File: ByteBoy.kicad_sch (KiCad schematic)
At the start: 10 parts, among them J1 1040310811 (SD Connector), J2 10118194-0001LF (USB-C Connec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, U1 ESP32-WROVER-E

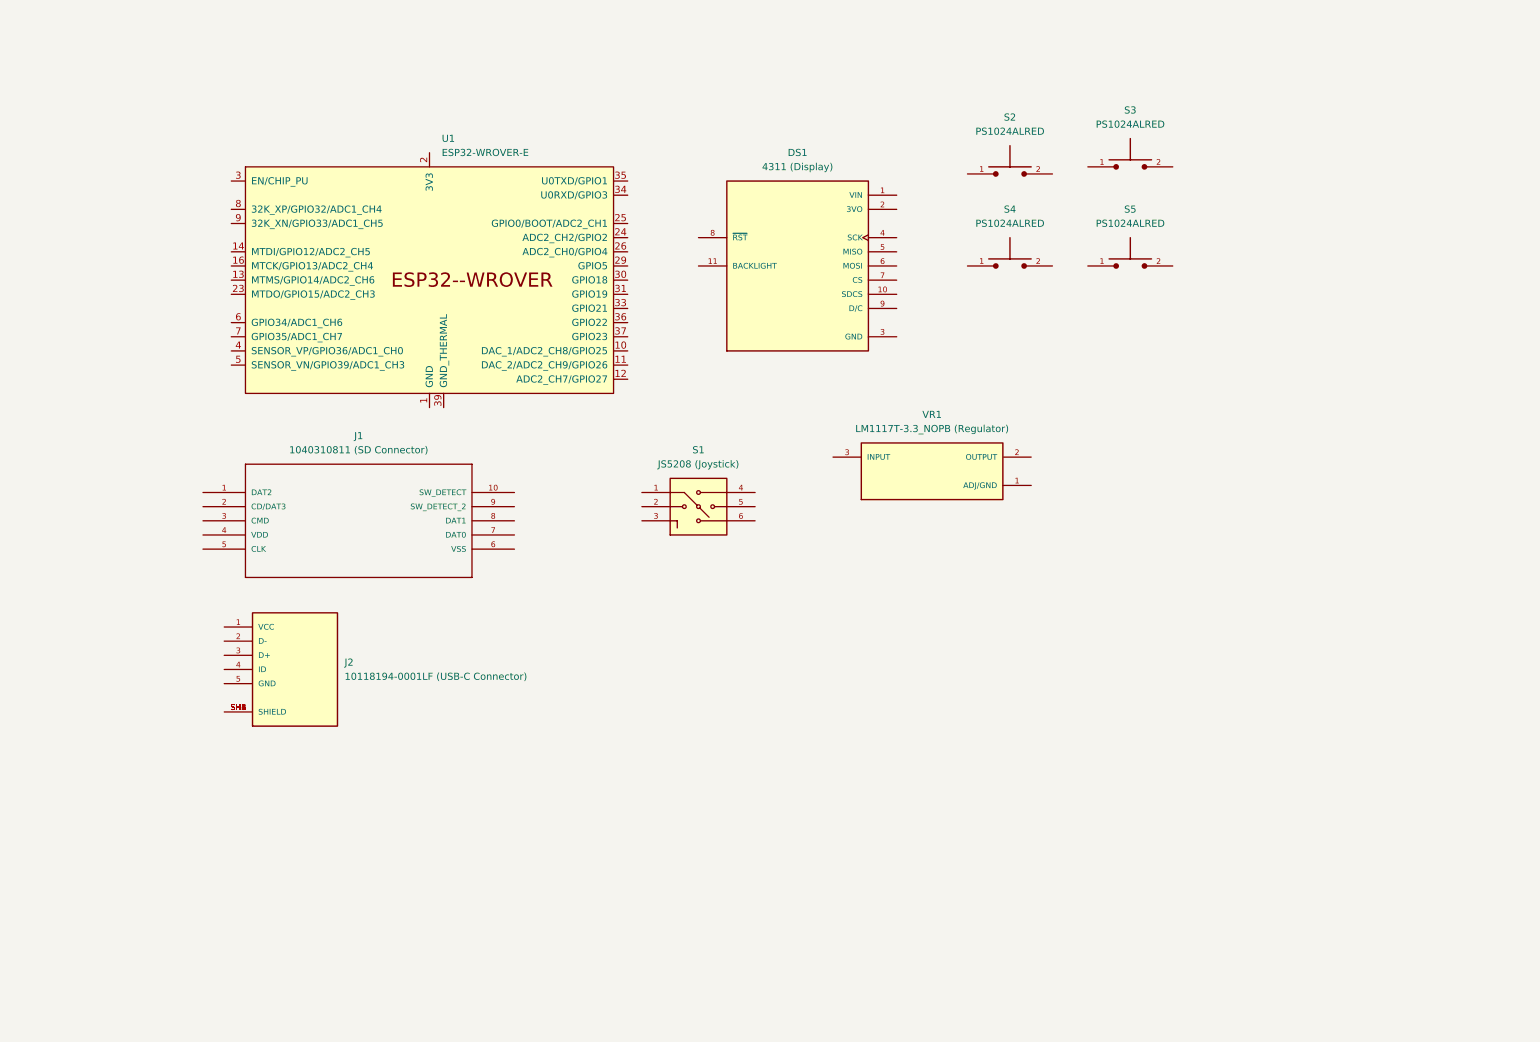
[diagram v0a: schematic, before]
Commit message: added usb to uart
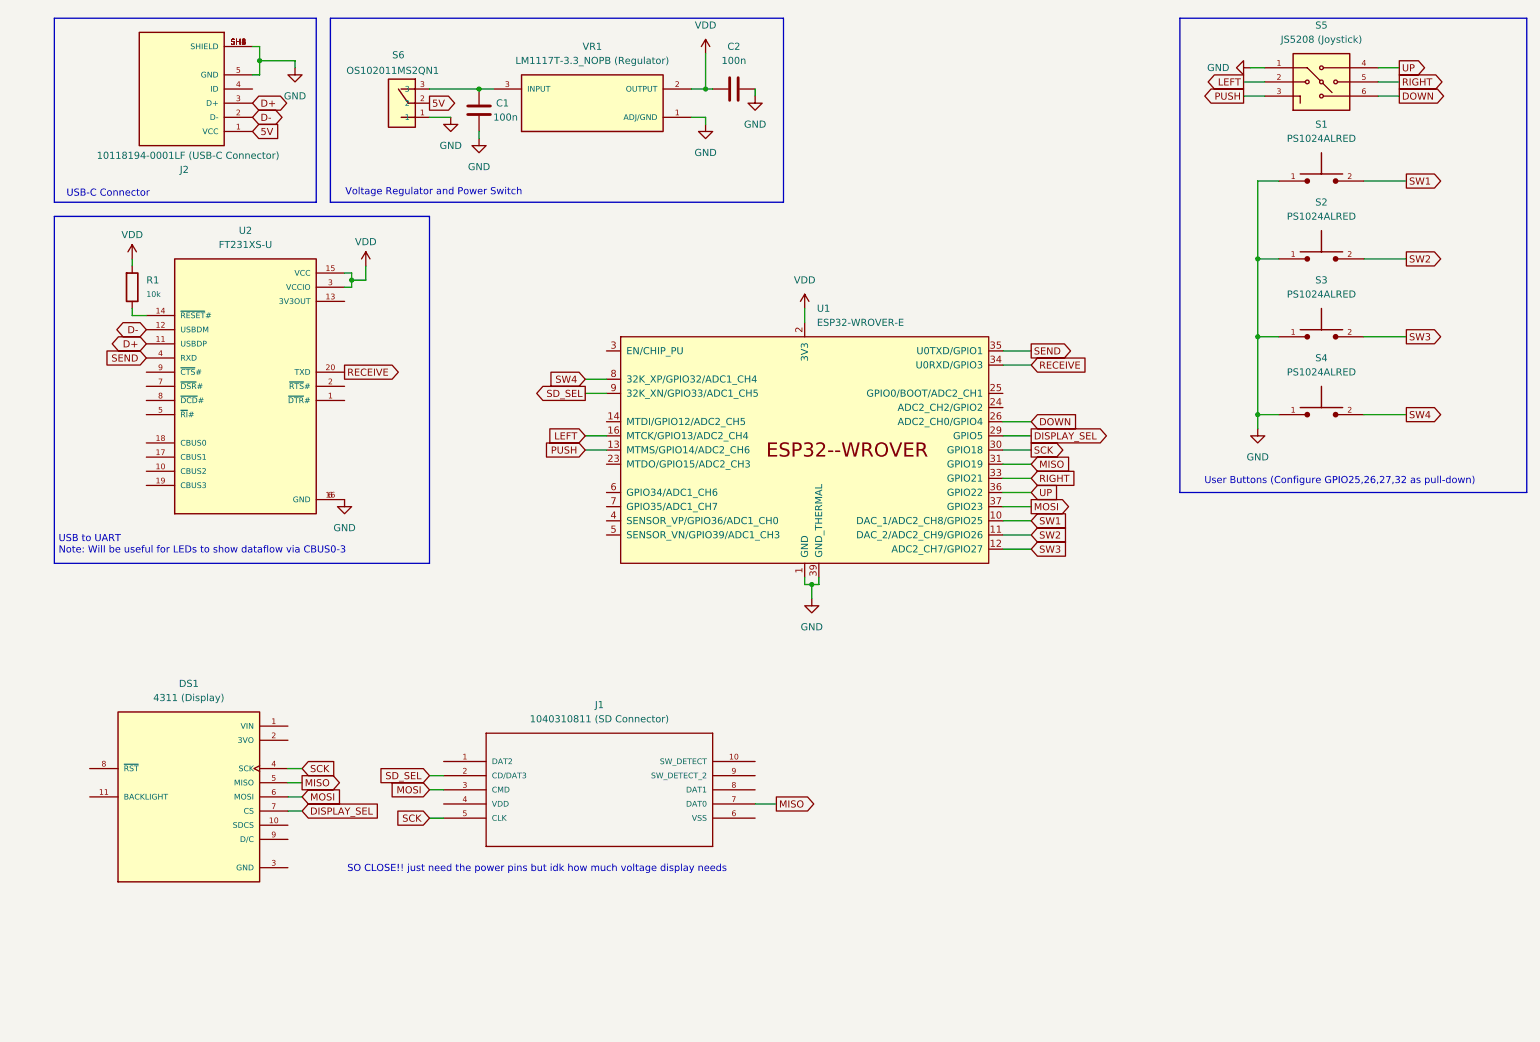
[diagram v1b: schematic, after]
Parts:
- added C1, C2: 100n, Capacitor_THT:C_Rect_L7.0mm_W2.5mm_P5.00mm, symbol enel200_uc_kicad7 (1):UC_C
- added R1: 10k, Resistor_THT:R_Axial_DIN0207_L6.3mm_D2.5mm_P7.62mm_Horizontal, symbol enel200_uc_kicad7 (1):UC_R
- added S6: OS102011MS2QN1, OS102011MS2QN1:SW_OS102011MS2QN1, symbol OS102011MS2QN1:OS102011MS2QN1
- added U2: FT231XS-U, FT231XS-U:SOP63P600X175-20N, symbol FT231XS-U:FT231XS-U
- renumbered S2 to S1, S3 to S2, S5 to S3, S1 to S5
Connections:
- net 5V: now reaches J2.1 (VCC)
- net 5V: now also S6.2
- net D-: now reaches J2.2 (D-)
- net D-: now also U2.12 (USBDM)
- net D+: now reaches J2.3 (D+)
- net D+: now also U2.11 (USBDP)
- net GND: now reaches J2.5 (GND)
- net GND: now also J2.SH1 (SHIELD), J2.SH2 (SHIELD), J2.SH3 (SHIELD), J2.SH4 (SHIELD), J2.SH5 (SHIELD), J2.SH6 (SHIELD), S1.1, S2.1, S3.1, S4.1, S5.1, U1.1 (GND), U1.15 (GND), U1.38 (GND), U1.39 (GND_THERMAL), VR1.1 (ADJ/GND), C1.1, C2.2, S6.1, U2.16 (GND), U2.6 (GND)
- net VDD: now reaches VR1.2 (OUTPUT)
- net VDD: now also U1.2 (3V3), C2.1, R1.1, U2.15 (VCC), U2.3 (VCCIO)
- net at VR1.3 (INPUT): now also C1.2, S6.3
- net SW1: now reaches U1.10 (DAC_1/ADC2_CH8/GPIO25)
- net SW1: now also S1.2
- net SW2: now reaches U1.11 (DAC_2/ADC2_CH9/GPIO26)
- net SW2: now also S2.2
- net SW3: now reaches U1.12 (ADC2_CH7/GPIO27)
- net SW3: now also S3.2
- net PUSH: now reaches U1.13 (MTMS/GPIO14/ADC2_CH6)
- net PUSH: now also S5.3
- net LEFT: now reaches U1.16 (MTCK/GPIO13/ADC2_CH4)
- net LEFT: now also S5.2
- net DOWN: now reaches U1.26 (ADC2_CH0/GPIO4)
- net DOWN: now also S5.6
- net DISPLAY_SEL: now reaches U1.29 (GPIO5)
- net DISPLAY_SEL: now also DS1.7 (CS)
- net SCK: now reaches U1.30 (GPIO18)
- net SCK: now also DS1.4 (SCK), J1.5 (CLK)
- net MISO: now reaches U1.31 (GPIO19)
- net MISO: now also DS1.5 (MISO), J1.7 (DAT0)
- net RIGHT: now reaches U1.33 (GPIO21)
- net RIGHT: now also S5.5
- net RECEIVE: now reaches U1.34 (U0RXD/GPIO3)
- net RECEIVE: now also U2.20 (TXD)
- net SEND: now reaches U1.35 (U0TXD/GPIO1)
- net SEND: now also U2.4 (RXD)
- net UP: now reaches U1.36 (GPIO22)
- net UP: now also S5.4
- net MOSI: now reaches U1.37 (GPIO23)
- net MOSI: now also DS1.6 (MOSI), J1.3 (CMD)
- net SW4: now reaches U1.8 (32K_XP/GPIO32/ADC1_CH4)
- net SW4: now also S4.2
- net SD_SEL: now reaches U1.9 (32K_XN/GPIO33/ADC1_CH5)
- net SD_SEL: now also J1.2 (CD/DAT3)
- new net: R1.2, U2.14 (~{RESET}#)
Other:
- note added: "SO CLOSE!! just need the power pins but idk how much voltage display needs"
- note added: "USB to UART Note: Will be useful for LEDs to show dataflow via CBUS0-3"
- note added: "USB-C Connector"
- note added: "User Buttons (Configure GPIO25,26,27,32 as pull-down)"
- note added: "Voltage Regulator and Power Switch"
- moved on the sheet: DS1, J1, J2, S1, S2, S3, S4, S5, U1, VR1

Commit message: adding decoupling
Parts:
- added C10: 1u, Capacitor_THT:C_Rect_L7.0mm_W2.5mm_P5.00mm, symbol enel200_uc_kicad7 (1):UC_C
- added C3, C5, C7, C9: 0.1u, Capacitor_THT:C_Rect_L7.0mm_W2.5mm_P5.00mm, symbol enel200_uc_kicad7 (1):UC_C
- added C4: 22u, Capacitor_THT:C_Rect_L7.0mm_W2.5mm_P5.00mm, symbol enel200_uc_kicad7 (1):UC_C
- added C6: 10u, Capacitor_THT:C_Rect_L7.0mm_W2.5mm_P5.00mm, symbol enel200_uc_kicad7 (1):UC_C
- added C8: 10uF, Capacitor_THT:C_Rect_L7.0mm_W2.5mm_P5.00mm, symbol enel200_uc_kicad7 (1):UC_C
- added D1, D2: UC_D, Diodes_THT:D_DO-35_SOD27_P2.54mm_Vertical_AnodeUp, symbol enel200_uc_kicad7 (1):UC_D
- added R2, R3: 5.1k, Resistor_THT:R_Axial_DIN0207_L6.3mm_D2.5mm_P7.62mm_Horizontal, symbol enel200_uc_kicad7 (1):UC_R
- added R4: 10k, Resistor_THT:R_Axial_DIN0207_L6.3mm_D2.5mm_P7.62mm_Horizontal, symbol enel200_uc_kicad7 (1):UC_R
- C1, C2: value 100n -> 10u
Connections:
- net 5V is gone; now on net +5V: J2.1 (VCC), S6.2
- net GND: now also C2.1, DS1.3 (GND), J1.6 (VSS), C10.2, C3.1, C5.2, C6.1, C7.2, C8.2, D1.1 (K), D2.1 (K); no longer C2.2
- net at U1.3 (EN/CHIP_PU): now also C10.1, R4.2
- net SD_DETECT: now reaches U1.4 (SENSOR_VP/GPIO36/ADC1_CH0)
- net SD_DETECT: now also J1.10 (SW_DETECT)
- net +3.3V: now reaches J1.4 (VDD)
- net +3.3V: now also C2.2, R1.1, U2.15 (VCC), U2.3 (VCCIO), VR1.2 (OUTPUT), C3.2, C4.1, C5.1, C9.1, R2.1, R4.1
- net +5V: now reaches DS1.1 (VIN)
- net +5V: now also C6.2, C7.1, C8.1, R3.1
- net DISPLAY_SEL renamed DISPLAY_SELECT
- net SD_SEL renamed SD_SELECT
- removed net VDD: C2.1, R1.1, U1.2 (3V3), U2.15 (VCC), U2.3 (VCCIO), VR1.2 (OUTPUT)
- new net: C4.2, C9.2, U1.2 (3V3)
- new net: D2.2 (A), R3.2
- new net: D1.2 (A), R2.2
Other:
- note added: "Display"
- note added: "User Buttons (Configure GPIO inputs as pull-down)"
- note added: "microSD card connector"
- note removed: "SO CLOSE!! just need the power pins but idk how much voltage display needs"
- note removed: "User Buttons (Configure GPIO25,26,27,32 as pull-down)"
- moved on the sheet: C1, DS1, J1, J2, S6, U1, VR1

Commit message: schematic done :)
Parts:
- added C11: 0.1u, Capacitor_THT:C_Rect_L7.0mm_W2.5mm_P5.00mm, symbol enel200_uc_kicad7 (1):UC_C
- added D3, D4, D5, D6: UC_D, Diodes_THT:D_DO-35_SOD27_P2.54mm_Vertical_AnodeUp, symbol enel200_uc_kicad7 (1):UC_D
- added DS2, DS3, DS4, DS5, DS6, DS7: UC_LED, LED_THT:LED_D5.0mm, symbol enel200_uc_kicad7 (1):UC_LED
- added R10, R11, R12, R13, R14, R5, R6, R7, R8, R9: 150, Resistor_THT:R_Axial_DIN0207_L6.3mm_D2.5mm_P7.62mm_Horizontal, symbol enel200_uc_kicad7 (1):UC_R
- added U3: 74HC151D_653, 74HC151D_653:SOIC127P600X175-16N, symbol 74HC151D_653:74HC151D_653
- R2: value 5.1k -> 150
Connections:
- net +3.3V: now also U1.2 (3V3), C11.2, R10.1, R5.2, R6.2, R7.2, R8.2, U3.16 (VCC)
- net DOWN: now also U3.3 (I1); no longer U1.26 (ADC2_CH0/GPIO4)
- net GND: now also C4.2, C9.2, C11.1, DS2.1 (K), DS3.1 (K), DS4.1 (K), DS5.1 (K), DS6.1 (K), U3.7 (~{E}), U3.8 (GND)
- net LEFT: now also U3.2 (I2); no longer U1.16 (MTCK/GPIO13/ADC2_CH4)
- net PUSH: now also U1.5 (SENSOR_VN/GPIO39/ADC1_CH3); no longer U1.13 (MTMS/GPIO14/ADC2_CH6)
- net RIGHT: now also U3.1 (I3); no longer U1.33 (GPIO21)
- net SD_DETECT: now also DS7.1 (K)
- net SW1: now also D3.1 (K), U3.15 (I4); no longer U1.10 (DAC_1/ADC2_CH8/GPIO25)
- net SW2: now also D4.1 (K), U3.14 (I5); no longer U1.11 (DAC_2/ADC2_CH9/GPIO26)
- net SW3: now also D5.1 (K), U3.13 (I6); no longer U1.12 (ADC2_CH7/GPIO27)
- net SW4: now also D6.1 (K), U3.12 (I7); no longer U1.8 (32K_XP/GPIO32/ADC1_CH4)
- net UP: now also U3.4 (I0); no longer U1.36 (GPIO22)
- new net: D5.2 (A), R7.1
- new net: D4.2 (A), R6.1
- new net: DS4.2 (A), R12.2
- new net: DS3.2 (A), R11.2
- new net: D6.2 (A), R8.1
- new net: DS7.2 (A), R10.2
- new net: DS6.2 (A), R14.2
- new net: D3.2 (A), R5.1
- new net: DS5.2 (A), R13.2
- new net: DS2.2 (A), R9.2
- new net LED1: R9.1, U1.26 (ADC2_CH0/GPIO4)
- new net LED2: R11.1, U1.16 (MTCK/GPIO13/ADC2_CH4)
- new net LED3: R12.1, U1.13 (MTMS/GPIO14/ADC2_CH6)
- new net LED4: R13.1, U1.33 (GPIO21)
- new net LED5: R14.1, U1.36 (GPIO22)
- new net MUX_OUT: U1.8 (32K_XP/GPIO32/ADC1_CH4), U3.5 (Y)
- new net MUX_S0: U1.10 (DAC_1/ADC2_CH8/GPIO25), U3.11 (S0)
- new net MUX_S1: U1.11 (DAC_2/ADC2_CH9/GPIO26), U3.10 (S1)
- new net MUX_S2: U1.12 (ADC2_CH7/GPIO27), U3.9 (S2)
- no-connect marks 0 -> 27
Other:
- note added: "8:1 multiplexer"
- note added: "LED Matrix"
- note added: "LEDs"
- company: (none) -> Auron Walker
- title: (none) -> Byte Boy
- moved on the sheet: C1, C10, C2, C4, C5, C6, C7, C8, C9, D1, D2, DS1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

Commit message: pcb layout
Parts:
- removed D1, D2, D3, D4, D5, D6: UC_D, Diodes_THT:D_DO-35_SOD27_P2.54mm_Vertical_AnodeUp, symbol enel200_uc_kicad7 (1):UC_D
- removed DS2, DS3, DS4, DS5, DS6, DS7: UC_LED, LED_THT:LED_D5.0mm, symbol enel200_uc_kicad7 (1):UC_LED
- added D1, D10, D11, D12, D2, D7, D8, D9: L-53GD, L-53GD:LEDRD254W50D500H1060, symbol L-53GD:L-53GD
- DS1: Description_1 Graphic LCD Display Module Red, Green, Blue (RGB) TFT - Color, IPS (In-Plane Switching) SPI 2 (50.80mm) 320 x 240 -> Graphic LCD Display Module Red, Green, Blue (RGB) TFT - Color, IPS (In-Plane Switching) SPI 2 (50.80mm) 320 x 240
- J1: Description_1 10 (8 + 2) Position Card Connector Secure Digital - microSD™ Surface Mount, Right Angle Gold -> 10 (8 + 2) Position Card Connector Secure Digital - microSD™ Surface Mount, Right Angle Gold
- J2: Description_1 Micro USB, Input Output Connectors, B TYPE RECEPTACLE with flange -> Micro USB, Input Output Connectors, B TYPE RECEPTACLE with flange
- R5, R6, R7, R8: value 150 -> 10k
- S1, S2, S3, S4: Description_1 Pushbutton Switch,PS1024 Series,SPST-NO,OFF-(ON),Round Red Cap,3A,125VAC,Solder | E-Switch PS1024ALRED -> Pushbutton Switch,PS1024 Series,SPST-NO,OFF-(ON),Round Red Cap,3A,125VAC,Solder | E-Switch PS1024ALRED
- S5: Description_1 Navigation Switch, JS1400 Series, 4-Way Directional, Plunger, 20mA DC, 12VDC | E-Switch JS5208 -> Navigation Switch, JS1400 Series, 4-Way Directional, Plunger, 20mA DC, 12VDC | E-Switch JS5208
- S6: Description_1 C & K Through Hole Slide Switch Single Pole Double Throw (SPDT) Latching 100 mA @ 12 V dc Slide -> C & K Through Hole Slide Switch Single Pole Double Throw (SPDT) Latching 100 mA @ 12 V dc Slide
- U2: Description_1 USB Full Speed to Full Handshake UART with USB Charger Detection | FTDI FT231XS-U -> USB Full Speed to Full Handshake UART with USB Charger Detection | FTDI FT231XS-U
- U3: Description_1 IC MULTIPLEXER 1 X 8:1 16-SO -> IC MULTIPLEXER 1 X 8:1 16-SO
- VR1: Description_1 800-mA 15-V linear voltage regulator -> 800-mA 15-V linear voltage regulator
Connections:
- net GND: now also D1.C, D10.C, D11.C, D2.C, D7.C, D8.C, D9.C
- net SD_DETECT: now also D12.C
- net SW1: now also R5.1
- net SW2: now also R6.1
- net SW3: now also R7.1
- net SW4: now also R8.1
- net at R12.2: now also D9.A
- net at R11.2: now also D8.A
- net at R10.2: now also D12.A
- net at R3.2: now also D1.A
- net at R14.2: now also D11.A
- net at R13.2: now also D10.A
- net at R2.2: now also D2.A
- net at R9.2: now also D7.A
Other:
- moved on the sheet: R11, R12, R13, R14, R5, R6, R7, R8, R9
